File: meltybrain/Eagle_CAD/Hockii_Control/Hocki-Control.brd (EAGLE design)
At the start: 90 x 46 mm, 78 parts, among them CN1 JST_2PIN, J1 SM03B-SRSS-TB(LF)(SN), J2 SM04B-SRSS-TB(LF)(SN), J4 SM04B-SRSS-TB(LF)(SN), J7 SM02B-SRSS-TB(LF)(SN), J8 SM02B-SRSS-TB(LF)(SN), U1 AP63200, U13 TMP235A4DCKR, U14 ADXL375, U15 NL27WZ32USG, U16 ADXL375, U17 ADXL375, U18 NL27WZ32USG, U19 ADXL375, U2 TEENSY_4.1, U3 AP2210K-5.0TRG1, U4 AP2210K-3.3TRG1, U5 TXS0104ED, U6 LDL212PU50R, U7 LIS3MDLTR

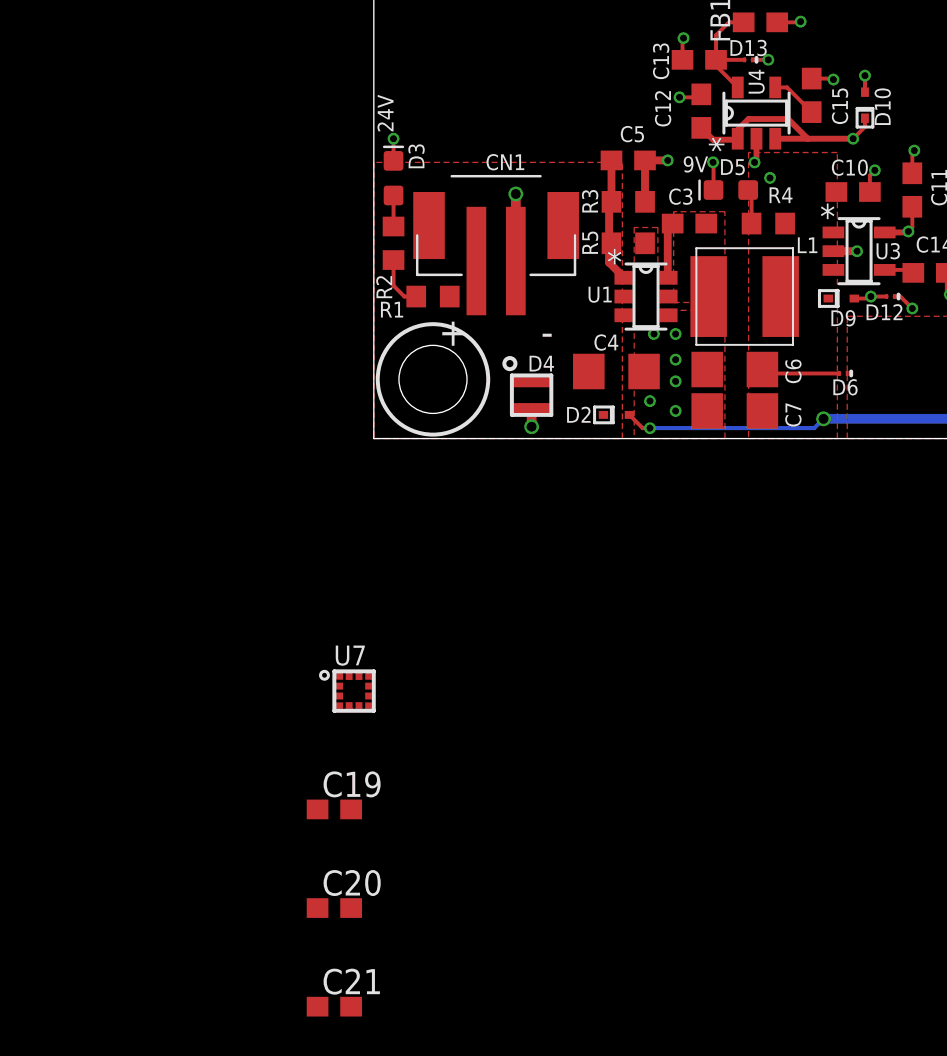
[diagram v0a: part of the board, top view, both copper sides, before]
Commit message: add replacement 9V regulator to schematic
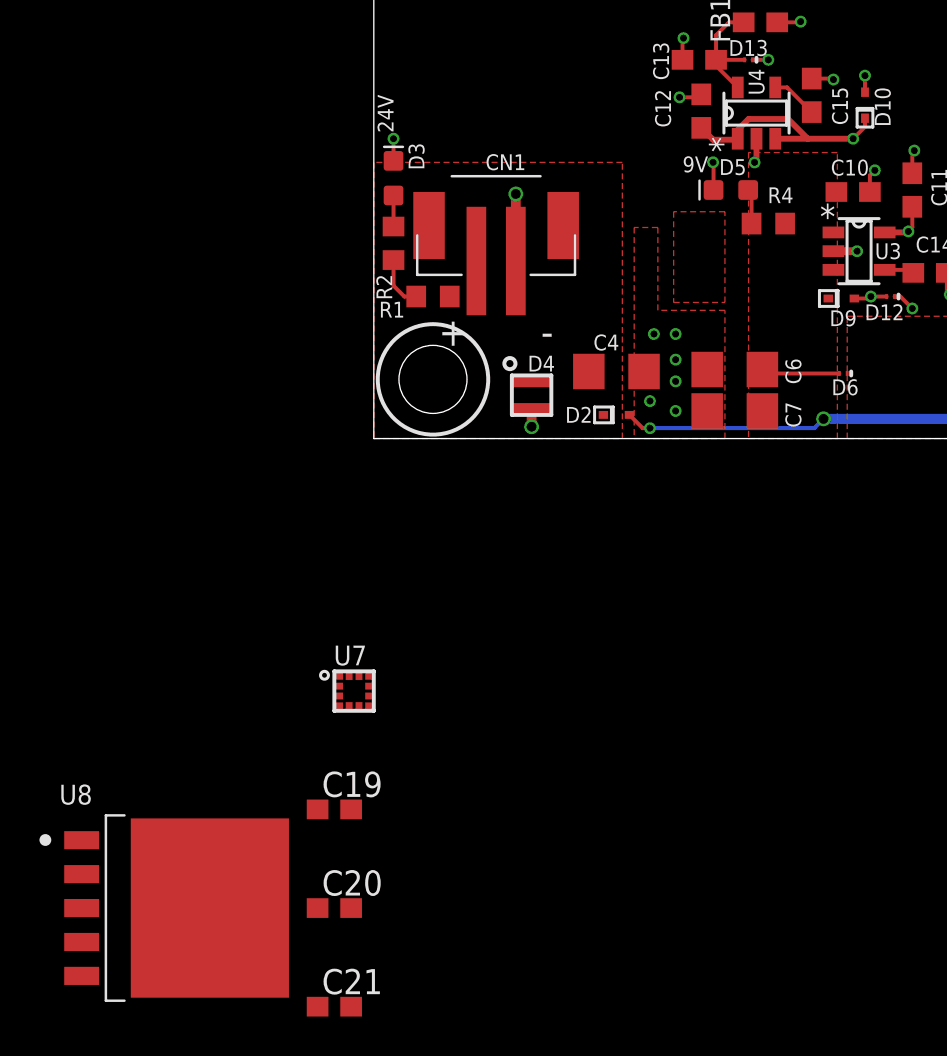
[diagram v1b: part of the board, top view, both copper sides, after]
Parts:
- removed C3: 0.1uF, rcl:C0603
- removed C5: 100pF, rcl:C0603
- removed L1: 10uH, Hocki_Library:LQH5BPN100M38L
- removed R3: 205k, rcl:R0603
- removed R5: 20k, rcl:R0603
- removed U1: AP63200, Hocki_Library:SOT-23-6
- added U8: BA50DD0WHFP-TR, Hocki_Library:HRP5
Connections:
- removed net N$1: C3.1, U1.6
- removed net N$12: C5.2, R3.2, R5.1, U1.1
- removed net N$3: C3.2, L1.1, U1.5
- net +24V: now also U8.1, U8.2; no longer U1.2, U1.3
- net 9V: now also U8.4; no longer C5.1, L1.2, R3.1
- net GND: now also U8.3, U8.6; no longer R5.2, U1.4
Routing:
- net 9V: track 101.1 -> 92.3 mm, vias 5 -> 3
- net N$12: track 6.45 -> 0.00 mm
- net N$1: track 2.85 -> 0.00 mm

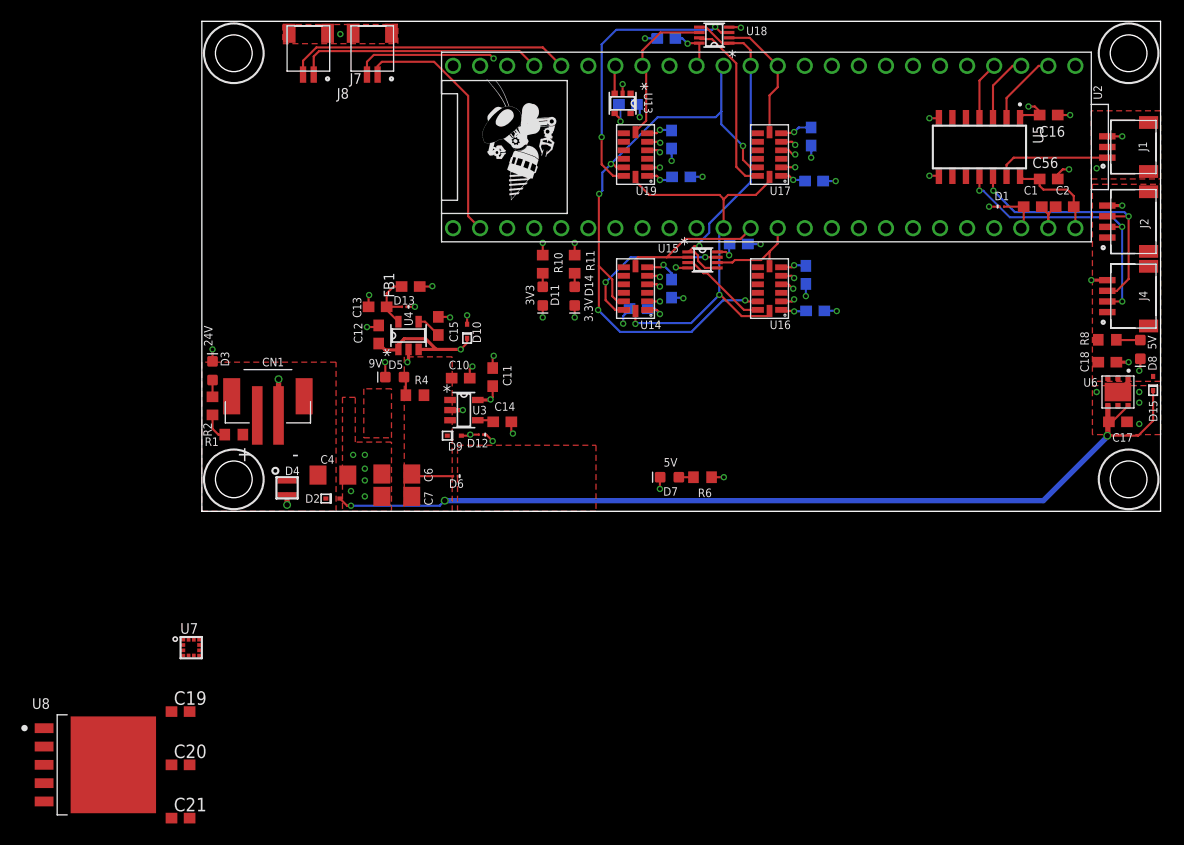
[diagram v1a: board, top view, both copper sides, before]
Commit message: begin rerouting new board
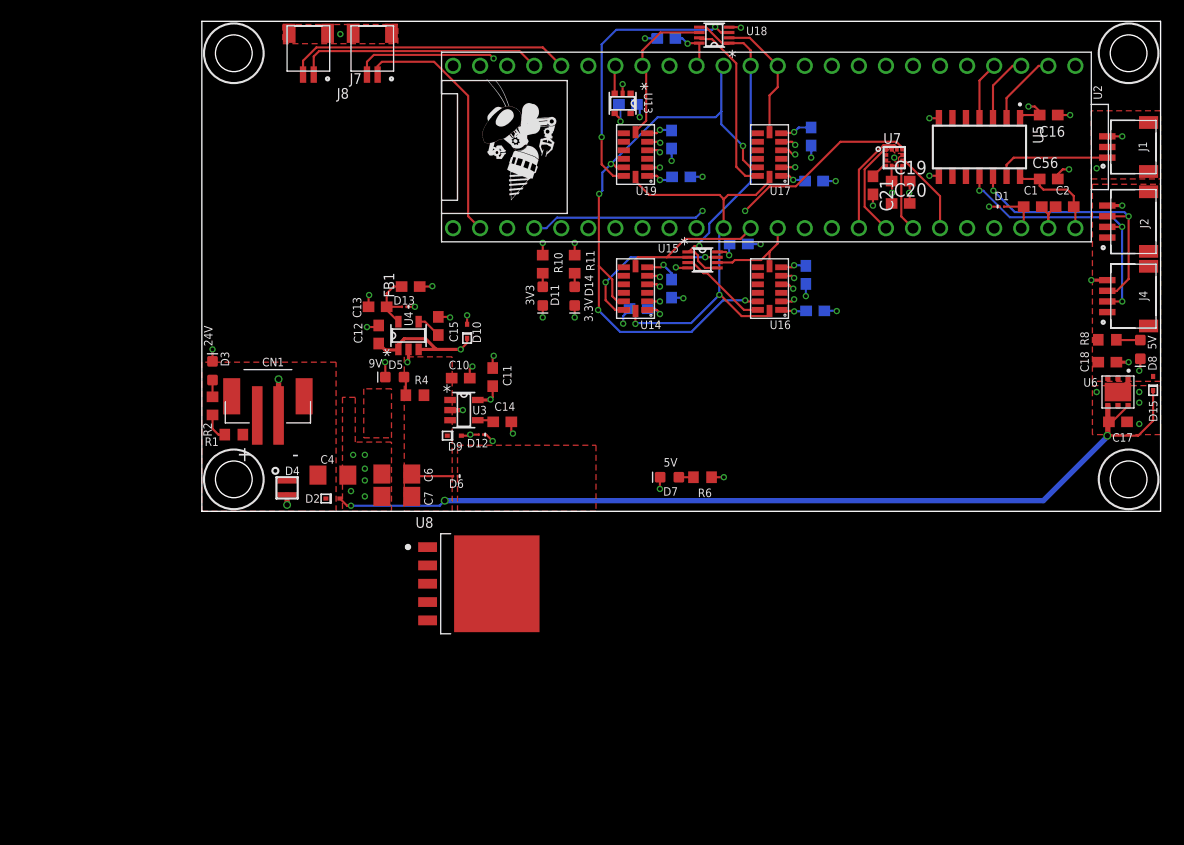
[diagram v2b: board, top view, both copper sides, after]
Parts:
- moved C21 88.1 mm to (11.0, 3.40), turned to 270 degrees
- moved C20 85.7 mm to (13.6, 1.70)
- moved C19 84.0 mm to (13.6, 3.80)
- moved U7 80.4 mm to (13.0, 6.00)
- moved U8 39.8 mm to (-26.0, -34.0)
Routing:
- net CS5: track 0.00 -> 38.3 mm, vias 0 -> 2
- net SDA: track 0.00 -> 10.3 mm
- net SCL: track 0.00 -> 9.15 mm
- net DRDY: track 0.00 -> 7.95 mm
- net INT: track 0.00 -> 6.36 mm
- net 3.3V: track 41.2 -> 45.3 mm, vias 14 -> 15
- net GND: track 71.3 -> 74.5 mm, vias 63 -> 65
- net N$5: track 0.00 -> 1.66 mm

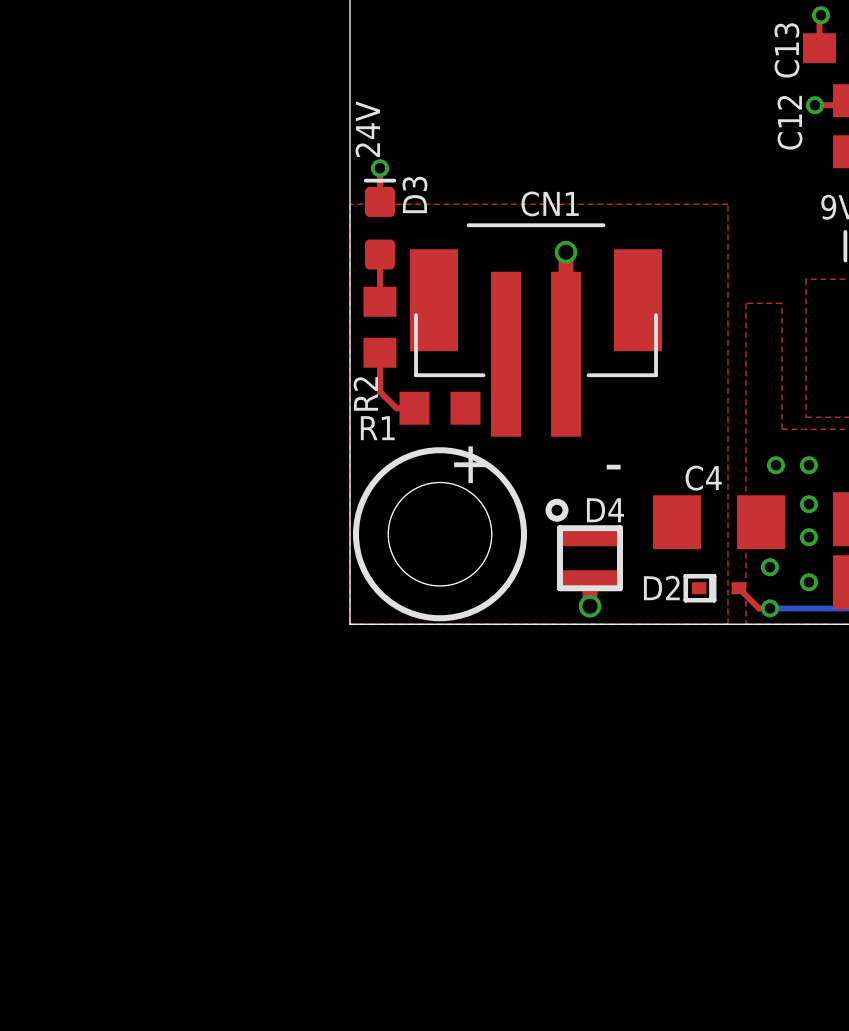
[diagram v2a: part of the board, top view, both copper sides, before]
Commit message: swap power connector
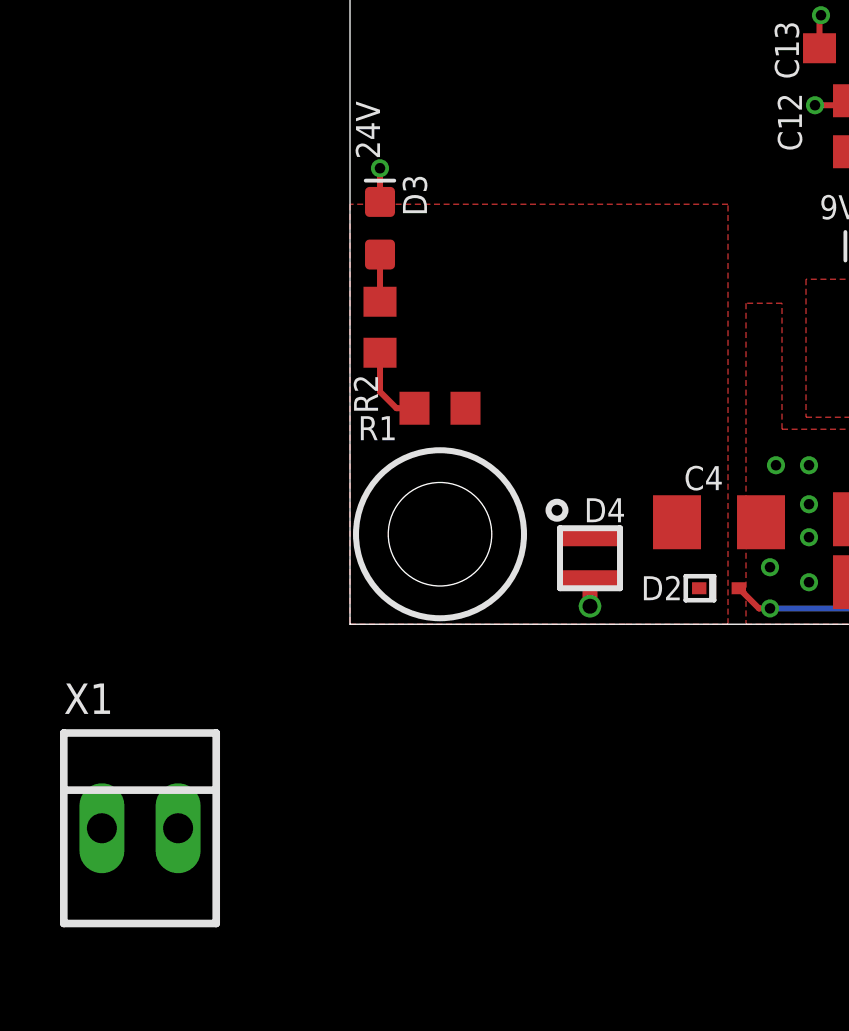
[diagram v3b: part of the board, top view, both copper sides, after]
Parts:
- removed CN1: JST_2PIN, Hocki_Library:JST-PH-2-SMT
- added X1: 22-23-2021, con-molex:22-23-2021
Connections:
- net +24V: now also X1.1; no longer CN1.1, CN1.NC1, CN1.NC2
- net GND: now also X1.2; no longer CN1.2
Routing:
- net GND: track 74.5 -> 71.1 mm, vias 65 -> 64
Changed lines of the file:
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@@
 <attribute name="VALUE" x="33.365" y="-20.705" size="1.27" layer="27"/>
-</element>
-<element name="CN1" library="Hocki_Library" package="JST-PH-2-SMT" package3d_urn="urn:adsk.eagle:package:22261884/2" value="JST_2PIN" x="-45.8" y="-16.4" smashed="yes">
-<attribute name="NAME" x="-46.34" y="-13.59" size="0.8" layer="25" font="vector" ratio="15"/>
-<attribute name="VALUE" x="-48.34" y="-24.02" size="1.27" layer="27" font="vector"/>
 </element>
 <element name="D4" library="Hocki_Library" package="D26V0H1U2LP20-7" value="D26V0H1U2LP20-7" x="-44" y="-25" smashed="yes" rot="R270">
@@
 <attribute name="NAME" x="-31.95" y="-28.75" size="1" layer="25" font="vector" ratio="10"/>
 <attribute name="VALUE" x="-31.95" y="-39.25" size="1" layer="27" font="vector" ratio="10" align="top-left"/>
+</element>
+<element name="X1" library="con-molex" library_urn="urn:adsk.eagle:library:165" package="22-23-2021" package3d_urn="urn:adsk.eagle:package:8078633/1" value="22-23-2021" x="-59" y="-34" smashed="yes">
+<attribute name="MF" value="MOLEX" x="-59" y="-34" size="1.778" layer="27" display="off"/>
+<attribute name="MPN" value="22-23-2021" x="-59" y="-34" size="1.778" layer="27" display="off"/>
+<attribute name="NAME" x="-61.54" y="-30.19" size="1.016" layer="25" ratio="10"/>
+<attribute name="OC_FARNELL" value="1462926" x="-59" y="-34" size="1.778" layer="27" display="off"/>
+<attribute name="OC_NEWARK" value="25C3832" x="-59" y="-34" size="1.778" layer="27" display="off"/>
+<attribute name="POPULARITY" value="40" x="-59" y="-34" size="1.778" layer="27" display="off"/>
+<attribute name="VALUE" x="-61.54" y="-39.08" size="1.016" layer="27" ratio="10"/>
 </element>
 </elements>
@@
 <via x="36" y="-17" extent="1-16" drill="0.35"/>
 <via x="36" y="-19" extent="1-16" drill="0.35"/>
-<contactref element="CN1" pad="2"/>
-<wire x1="-44.8" y1="-18.2" x2="-44.8" y2="-14.8" width="0.5" layer="1"/>
-<via x="-44.8" y="-14.8" extent="1-16" drill="0.5"/>
 <via x="-1.4" y="18.2" extent="1-16" drill="0.35"/>
 <wire x1="-8.975096875" y1="7.4" x2="-9.065028125" y2="7.4899875" width="0.2" layer="1"/>
@@
 <via x="14.4" y="2.7" extent="1-16" drill="0.35"/>
 <wire x1="14.45" y1="1.7" x2="14.45" y2="2.75" width="0.2" layer="1"/>
+<contactref element="X1" pad="2"/>
+<wire x1="-44" y1="-26.6" x2="-57.73" y2="-34" width="0" layer="19" extent="1-1"/>
 <wire x1="-38.3" y1="-23.8" x2="-44" y2="-25.675" width="0" layer="19" extent="1-1"/>
 <wire x1="-38" y1="-25.3" x2="-38.3" y2="-23.8" width="0" layer="19" extent="1-1"/>
@@
 <wire x1="33" y1="1.5" x2="28.15" y2="1.4" width="0" layer="19" extent="1-1"/>
 <wire x1="31.5" y1="-5.5" x2="27.46" y2="-0.62" width="0" layer="19" extent="1-1"/>
-<wire x1="-44.8" y1="-18.2" x2="-44" y2="-25.675" width="0" layer="19" extent="1-1"/>
-<wire x1="-51" y1="-13.123" x2="-44.8" y2="-14.8" width="0" layer="19" extent="1-1"/>
 <wire x1="33.85" y1="-13.2" x2="33" y2="-5.5" width="0" layer="19" extent="1-1"/>
 <wire x1="36.1" y1="-12.877" x2="35" y2="-13.2" width="0" layer="19" extent="1-1"/>
@@
 <wire x1="-30.81" y1="-34" x2="-35.1" y2="-25.8" width="0" layer="19" extent="1-1"/>
 <wire x1="-24.31" y1="-34" x2="-30.81" y2="-34" width="0" layer="19" extent="1-1"/>
+<wire x1="-51" y1="-13.123" x2="-44" y2="-25.675" width="0" layer="19" extent="1-1"/>
 <wire x1="-8.977" y1="-24" x2="-22.8" y2="-19.9" width="0" layer="19" extent="1-1"/>
 <wire x1="-34.2" y1="17.675" x2="-12.5" y2="12.9" width="0" layer="19" extent="1-1"/>
@@
 <vertex x="-39.4" y="-27.2"/>
 </polygon>
-<contactref element="CN1" pad="NC2"/>
-<contactref element="CN1" pad="NC1"/>
-<contactref element="CN1" pad="1"/>
 <contactref element="D4" pad="1"/>
 <contactref element="D2" pad="1"/>
@@
 <contactref element="U8" pad="2"/>
 <contactref element="U8" pad="1"/>
-<wire x1="-30.81" y1="-30.56" x2="-30.81" y2="-32.28" width="0" layer="19" extent="1-1"/>
-<wire x1="-44" y1="-24.325" x2="-30.81" y2="-30.56" width="0" layer="19" extent="1-1"/>
+<contactref element="X1" pad="1"/>
+<wire x1="-48.15" y1="-20" x2="-60.27" y2="-34" width="0" layer="19" extent="1-1"/>
+<wire x1="-44" y1="-24.325" x2="-48.15" y2="-20" width="0" layer="19" extent="1-1"/>
 <wire x1="-41.1" y1="-23.8" x2="-44" y2="-24.325" width="0" layer="19" extent="1-1"/>
 <wire x1="-40.36" y1="-26" x2="-41.1" y2="-23.8" width="0" layer="19" extent="1-1"/>
-<wire x1="-48.15" y1="-20" x2="-44" y2="-24.325" width="0" layer="19" extent="1-1"/>
-<wire x1="-46.8" y1="-18.2" x2="-48.15" y2="-20" width="0" layer="19" extent="1-1"/>
-<wire x1="-49.2" y1="-16.4" x2="-46.8" y2="-18.2" width="0" layer="19" extent="1-1"/>
-<wire x1="-42.4" y1="-16.4" x2="-46.8" y2="-18.2" width="0" layer="19" extent="1-1"/>
+<wire x1="-30.81" y1="-30.56" x2="-40.36" y2="-26" width="0" layer="19" extent="1-1"/>
+<wire x1="-30.81" y1="-32.28" x2="-30.81" y2="-30.56" width="0" layer="19" extent="1-1"/>
 </signal>
 <signal name="5V_RC_SIGNAL">

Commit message: order Hockii v1
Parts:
- removed C12: 1uF, rcl:C0603
- removed C13: 2.2uF, rcl:C0603
- removed C15: 100pF, rcl:C0603
- removed D10: BAS581-02V-V-G-08, Hocki_Library:SOD-523
- removed D11: GREEN, SparkFun-LED:LED-0603
- removed D13: PESD4V0Y1BSFYL, Hocki_Library:DSN0603-2
- removed FB1: MPZ1608R391ATD25, Hocki_Library:0603
- removed R10: 169, rcl:R0603
- removed U4: AP2210K-3.3TRG1, Hocki_Library:SOT-23-5
- added C3: 0.1uF, rcl:C0603
- added U$1: (no value), RoboJackets-Aesthetics:ROBOBUZZ_0.6X
- moved X1 72.6 mm to (7.70, -5.40), turned to 180 degrees
- moved C4 57.8 mm to (14.4, -3.40)
- moved D4 56.4 mm to (10.0, -8.60)
- moved R1 56.1 mm to (6.00, -9.00)
- moved R2 54.5 mm to (3.00, -10.2), turned to 0 degrees
- moved D3 54.1 mm to (3.00, -11.6), turned to 0 degrees
- moved D2 50.6 mm to (8.30, -9.90), turned to 270 degrees
- moved U8 50.3 mm to (17.9, -9.40)
- moved C7 46.1 mm to (10.8, -13.7), turned to 270 degrees
- moved C6 42.7 mm to (7.80, -13.7), turned to 270 degrees
- moved D6 38.8 mm to (9.30, -14.1), turned to 90 degrees
- moved R4 37.7 mm to (5.70, -15.1), turned to 90 degrees
- moved D5 36.9 mm to (3.00, -13.8), turned to 0 degrees
- moved C10 26.6 mm to (-1.30, -11.5), turned to 270 degrees
- moved C11 24.3 mm to (-0.40, -14.1), turned to 0 degrees
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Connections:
- removed net +3V3: D10.2, FB1.2, R10.2
- removed net N$11: C15.1, U4.4
- removed net N$17: D11.A, R10.1
- removed net N$28: C13.1, D13.C2, FB1.1, U4.5
- net 3.3V: now also C3.1
- net 5V: no longer C12.1, D10.1, U4.1, U4.3
- net GND: now also C3.2; no longer C12.2, C13.2, C15.2, D11.C, D13.C1, U4.2
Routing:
- net 9V: track 92.3 -> 6.93 mm, vias 3 -> 1
- net GND: track 71.1 -> 101.8 mm, vias 64 -> 52
- net ESC_TEL_R: track 23.7 -> 6.06 mm
- net 5V: track 34.0 -> 23.3 mm, vias 5 -> 4
- net ESC_TEL_L: track 26.8 -> 18.1 mm
- net ESC_L: track 23.2 -> 16.1 mm
- net SCL: track 9.15 -> 2.27 mm
- net SDA: track 10.3 -> 3.63 mm
- net N$28: track 6.22 -> 0.00 mm
- net CS5: track 38.3 -> 33.4 mm, vias 2 -> 1
- net N$15: track 1.37 -> 5.67 mm
- net DRDY: track 7.95 -> 11.8 mm
- net 3.3V: track 45.3 -> 49.0 mm, vias 15 -> 16
- net +3V3: track 3.19 -> 0.00 mm, vias 3 -> 0
- net N$18: track 1.77 -> 4.75 mm
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- removed copper zone on layer 1, net N$3
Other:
- board size 90 x 46 mm -> 74 x 37 mm
- board text added: "Hockii"
- board text added: "Hockii Control V1"
- board text removed: "Hocki Control V2"
